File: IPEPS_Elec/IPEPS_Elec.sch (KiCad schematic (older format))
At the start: 35 parts

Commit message: reorganise components
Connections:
- net at SW?.2, U?.1, U?.11 (3C)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: now also R?.2
- net Out_C: no longer names the net of R?.2, U?.12 (1Y)
- net Out_L: no longer names the net of R?.2, U?.12 (1Y)
- net Out_RJ: no longer names the net of R?.2, U?.6 (2Y)
- net Out_T: no longer names the net of R?.2, U?.6 (2Y)
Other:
- moved on the sheet: BAT?, C?, D?, Q?, R?, SW?, U?, U?A

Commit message: reorganise wiring
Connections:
- net IN_J: now also U?.2 (1B); no longer U?.13 (1C)
- net at R?.2, SW?.2, U?.1 (1A)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: now also U?.3 (2A); no longer U?.1 (1A)
- net at R?.2, SW?.2, U?.1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: now also U?.1 (1A); no longer U?.3 (2A)
- net at U?.4 (2Y): now also U?.4 (2B); no longer U?.2 (1B)
- net at U?.2 (1Y): now also U?.13 (1C); no longer U?.4 (2B)
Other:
- moved on the sheet: BAT?, C?, D?, Q?, R?, SW?, U?, U?A

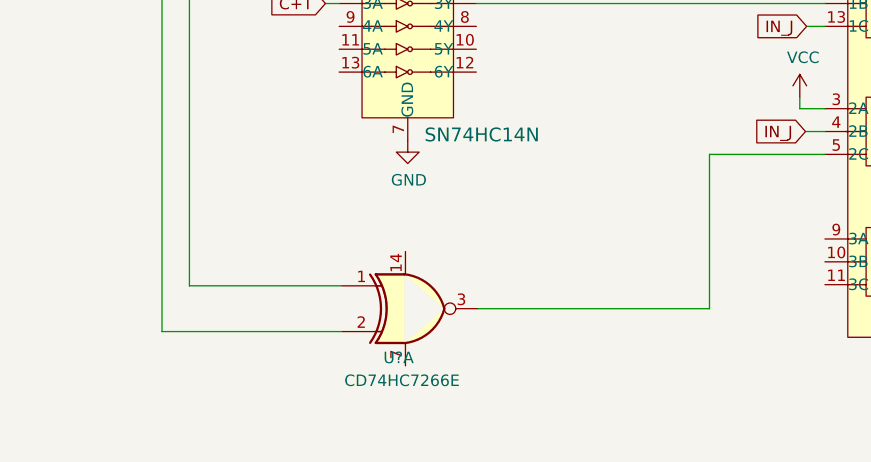
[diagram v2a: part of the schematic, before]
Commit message: add missing pins to XNOR gate
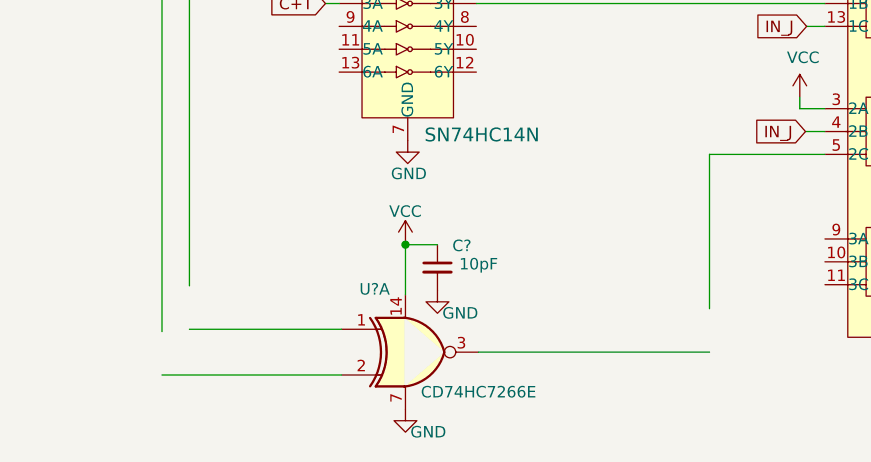
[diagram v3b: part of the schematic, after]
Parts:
- added C?: 10pF, symbol Device:C_Small
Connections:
- wire segments 88 -> 91
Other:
- moved on the sheet: U?A
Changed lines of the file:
@@
 P 6530 5210
 F 0 "#PWR?" H 6530 4960 50  0001 C CNN
-F 1 "GND" H 6535 5037 50  0000 C CNN
+F 1 "GND" H 6535 5065 50  0000 C CNN
 F 2 "" H 6530 5210 50  0001 C CNN
 F 3 "" H 6530 5210 50  0001 C CNN
@@
 $EndComp
 $Comp
-L IPEPS_Elec:CD74HC7266E U?
-U 1 1 6192A273
-P 6540 5945
-F 0 "U?" H 6490 5730 50  0000 C CNN
-F 1 "CD74HC7266E" H 6505 5630 50  0000 C CNN
-F 2 "Package_DIP:DIP-14_W7.62mm" H 6530 5645 50  0001 C CNN
-F 3 "https://www.ti.com/lit/ds/symlink/cd74hc7266.pdf" H 6540 5945 50  0001 C CNN
-	1    6540 5945
-	1    0    0    -1
-$EndComp
-$Comp
 L dk_Logic-Gates-and-Inverters:SN74HC14N U?
 U 1 1 6186B77E
@@
 	6170 4610 6230 4610
 Wire Wire Line
-	5575 5845 6240 5845
-Wire Wire Line
-	5455 6045 6240 6045
+	5575 6035 6240 6035
+Wire Wire Line
+	5455 6235 6240 6235
 Wire Wire Line
 	4450 1595 4450 1445
@@
 	6830 4610 8355 4610
 Wire Wire Line
-	6840 5945 7850 5945
+	6840 6135 7850 6135
 $Comp
 L Switch:SW_SPDT SW?
@@
 Wire Wire Line
 	5825 1795 6225 1795
+$Comp
+L Device:C_Small C?
+U 1 1 61C9858D
+P 6660 5765
+F 0 "C?" H 6725 5860 50  0000 L CNN
+F 1 "10pF" H 6755 5780 50  0000 L CNN
+F 2 "" H 6660 5765 50  0001 C CNN
+F 3 "~" H 6660 5765 50  0001 C CNN
+	1    6660 5765
+	1    0    0    -1
+$EndComp
+$Comp
+L power:VCC #PWR?
+U 1 1 61C97F67
+P 6520 5660
+F 0 "#PWR?" H 6520 5510 50  0001 C CNN
+F 1 "VCC" H 6520 5800 50  0000 C CNN
+F 2 "" H 6520 5660 50  0001 C CNN
+F 3 "" H 6520 5660 50  0001 C CNN
+	1    6520 5660
+	1    0    0    -1
+$EndComp
+Wire Wire Line
+	6520 5885 6520 5665
+Wire Wire Line
+	6660 5665 6520 5665
+Connection ~ 6520 5665
+Wire Wire Line
+	6520 5665 6520 5660
+$Comp
+L power:GND #PWR?
+U 1 1 61CAB77E
+P 6660 5865
+F 0 "#PWR?" H 6660 5615 50  0001 C CNN
+F 1 "GND" H 6760 5765 50  0000 C CNN
+F 2 "" H 6660 5865 50  0001 C CNN
+F 3 "" H 6660 5865 50  0001 C CNN
+	1    6660 5865
+	1    0    0    -1
+$EndComp
+$Comp
+L IPEPS_Elec:CD74HC7266E U?
+U 1 1 6192A273
+P 6540 6135
+F 0 "U?" H 6385 6410 50  0000 C CNN
+F 1 "CD74HC7266E" H 6840 5960 50  0000 C CNN
+F 2 "Package_DIP:DIP-14_W7.62mm" H 6530 5835 50  0001 C CNN
+F 3 "https://www.ti.com/lit/ds/symlink/cd74hc7266.pdf" H 6540 6135 50  0001 C CNN
+	1    6540 6135
+	1    0    0    -1
+$EndComp
+$Comp
+L power:GND #PWR?
+U 1 1 61CAD1FF
+P 6520 6385
+F 0 "#PWR?" H 6520 6135 50  0001 C CNN
+F 1 "GND" H 6620 6285 50  0000 C CNN
+F 2 "" H 6520 6385 50  0001 C CNN
+F 3 "" H 6520 6385 50  0001 C CNN
+	1    6520 6385
+	1    0    0    -1
+$EndComp
 $EndSCHEMATC
